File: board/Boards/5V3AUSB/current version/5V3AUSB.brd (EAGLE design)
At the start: 53.3 x 32.7 mm, 12 parts

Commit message: getting ready to add pads out +5V
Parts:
- added TP1, TP2: TP2P2-38-20, testpad:P2-38-20
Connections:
- net GND: now also TP1.TP-2, TP2.TP-2
- net N$3: now also TP1.TP-1, TP2.TP-1
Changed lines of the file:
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@@
 <element name="R1" library="resistor" package="R1206" value="250" x="11.43" y="2.54"/>
 <element name="U$1" library="Molex" package="2X2MOLEX" value="2X2-MOLEX" x="15.24" y="24.13" rot="R270"/>
+<element name="TP1" library="testpad" package="P2-38-20" value="TP2P2-38-20" x="-17.78" y="0">
+<attribute name="TP_SIGNAL_NAME" value="" x="-17.78" y="0" size="1.778" layer="27" display="off"/>
+</element>
+<element name="TP2" library="testpad" package="P2-38-20" value="TP2P2-38-20" x="-2.54" y="-17.78">
+<attribute name="TP_SIGNAL_NAME" value="" x="-2.54" y="-17.78" size="1.778" layer="27" display="off"/>
+</element>
 </elements>
 <signals>
@@
 <via x="29.21" y="22.86" extent="1-16" drill="0.6"/>
 <via x="29.21" y="21.59" extent="1-16" drill="0.6"/>
+<contactref element="TP1" pad="TP-2"/>
+<contactref element="TP2" pad="TP-2"/>
+<wire x1="-15.875" y1="0" x2="-0.635" y2="-17.78" width="0" layer="19" extent="1-1"/>
+<wire x1="10.008" y1="2.54" x2="-15.875" y2="0" width="0" layer="19" extent="1-1"/>
 </signal>
 <signal name="N$2">
@@
 <wire x1="29.21" y1="2.54" x2="29.21" y2="1.27" width="2.1844" layer="1"/>
 <via x="29.21" y="1.27" extent="1-16" drill="0.6"/>
+<contactref element="TP1" pad="TP-1"/>
+<contactref element="TP2" pad="TP-1"/>
+<wire x1="-19.685" y1="0" x2="-4.445" y2="-17.78" width="0" layer="19" extent="1-1"/>
+<wire x1="6.52" y1="12.39" x2="-19.685" y2="0" width="0" layer="19" extent="1-1"/>
 </signal>
 <signal name="N$6">

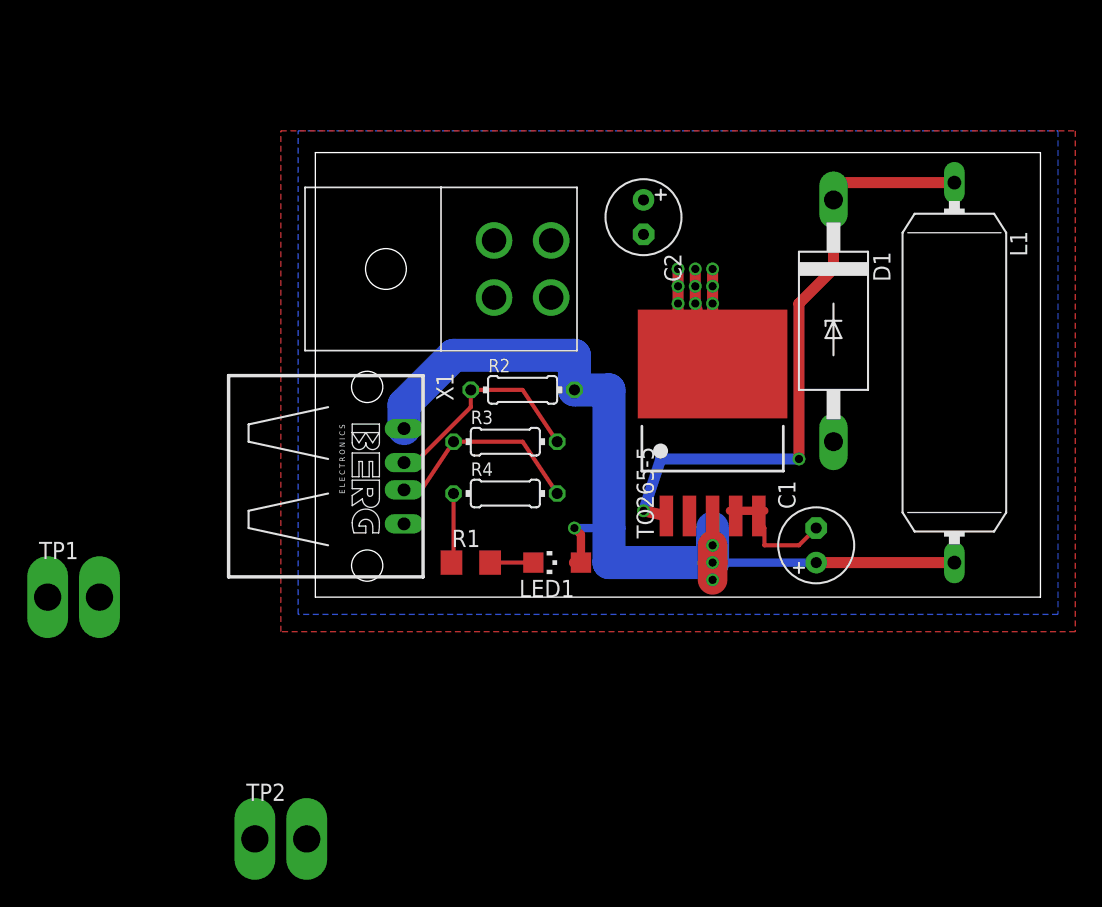
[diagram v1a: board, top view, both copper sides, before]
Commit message: board placement is looking good. going to verify schematic now
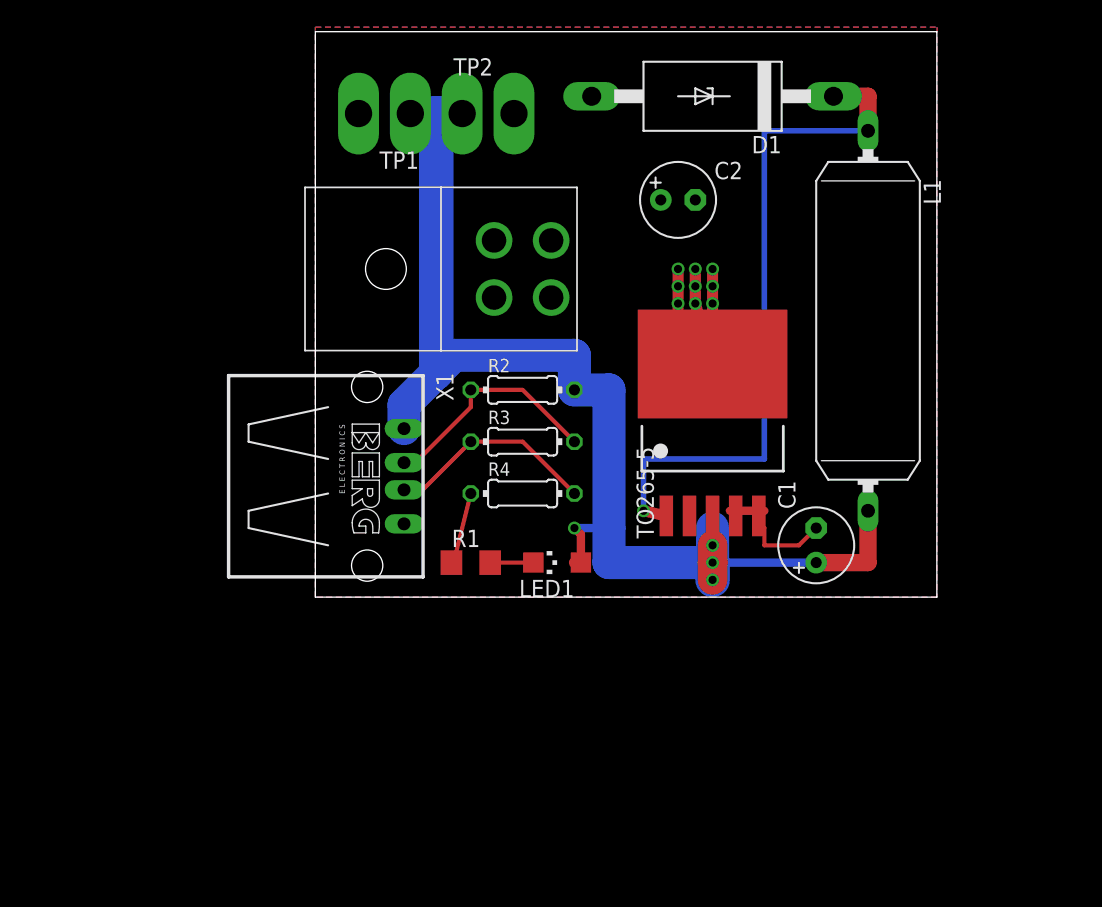
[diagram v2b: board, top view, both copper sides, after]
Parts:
- moved TP2 55.5 mm to (12.7, 35.6)
- moved TP1 42.3 mm to (5.08, 35.6), turned to 180 degrees
- moved D1 18.8 mm to (29.2, 36.8), turned to 180 degrees
- moved L1 7.41 mm to (40.6, 20.3)
- moved C2 2.84 mm to (26.7, 29.2), turned to 0 degrees
- moved R3 1.27 mm to (15.2, 11.4)
- moved R4 1.27 mm to (15.2, 7.62)
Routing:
- net N$3: track 72.0 -> 95.5 mm
- net N$2: track 46.2 -> 51.3 mm, vias 2 -> 1
- net N$7: track 16.2 -> 17.0 mm
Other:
- board size 53.3 x 32.7 mm -> 45.7 x 41.6 mm
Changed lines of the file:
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@@
 <board>
 <plain>
-<wire x1="0" y1="0" x2="53.32" y2="0" width="0" layer="20"/>
-<wire x1="53.32" y1="0" x2="53.32" y2="32.69" width="0" layer="20"/>
-<wire x1="53.32" y1="32.69" x2="0" y2="32.69" width="0" layer="20"/>
-<wire x1="0" y1="32.69" x2="0" y2="0" width="0" layer="20"/>
+<wire x1="0" y1="0" x2="45.7" y2="0" width="0" layer="20"/>
+<wire x1="45.7" y1="0" x2="45.7" y2="41.58" width="0" layer="20"/>
+<wire x1="45.7" y1="41.58" x2="0" y2="41.58" width="0" layer="20"/>
+<wire x1="0" y1="41.58" x2="0" y2="0" width="0" layer="20"/>
 </plain>
 <attributes>
@@
 <elements>
 <element name="C1" library="resistor" package="E2,5-6" value="220uF" x="36.83" y="3.81" rot="R90"/>
-<element name="C2" library="resistor" package="E2,5-6" value="470uF" x="24.13" y="27.94" rot="R270"/>
-<element name="D1" library="diode" package="CB429-17" value="15KEXX" x="38.1" y="20.32" rot="R270"/>
-<element name="L1" library="inductors" package="SUKW3-27" value="22uH" x="46.99" y="16.51" rot="R270"/>
+<element name="C2" library="resistor" package="E2,5-6" value="470uF" x="26.67" y="29.21"/>
+<element name="D1" library="diode" package="CB429-17" value="15KEXX" x="29.21" y="36.83" rot="R180"/>
+<element name="L1" library="inductors" package="SUKW3-27" value="22uH" x="40.64" y="20.32" rot="R270"/>
 <element name="TO265-5" library="on-semiconductor" package="TO263_5" value="CAT4101" x="29.21" y="13.97">
 <attribute name="OC_NEWARK" value="08R5264" x="48.26" y="3.81" size="1.778" layer="27" display="off"/>
@@
 <attribute name="SPICEPREFIX" value="R" x="15.24" y="15.24" size="1.778" layer="27" display="off"/>
 </element>
-<element name="R3" library="eagle-ltspice" package="0204/7" value="" x="13.97" y="11.43">
-<attribute name="SPICEMODEL" value="NONE" x="13.97" y="11.43" size="1.778" layer="27" display="off"/>
-<attribute name="SPICEPREFIX" value="R" x="13.97" y="11.43" size="1.778" layer="27" display="off"/>
-</element>
-<element name="R4" library="eagle-ltspice" package="0204/7" value="" x="13.97" y="7.62">
-<attribute name="SPICEMODEL" value="NONE" x="13.97" y="7.62" size="1.778" layer="27" display="off"/>
-<attribute name="SPICEPREFIX" value="R" x="13.97" y="7.62" size="1.778" layer="27" display="off"/>
+<element name="R3" library="eagle-ltspice" package="0204/7" value="" x="15.24" y="11.43">
+<attribute name="SPICEMODEL" value="NONE" x="15.24" y="11.43" size="1.778" layer="27" display="off"/>
+<attribute name="SPICEPREFIX" value="R" x="15.24" y="11.43" size="1.778" layer="27" display="off"/>
+</element>
+<element name="R4" library="eagle-ltspice" package="0204/7" value="" x="15.24" y="7.62">
+<attribute name="SPICEMODEL" value="NONE" x="15.24" y="7.62" size="1.778" layer="27" display="off"/>
+<attribute name="SPICEPREFIX" value="R" x="15.24" y="7.62" size="1.778" layer="27" display="off"/>
 </element>
 <element name="LED1" library="led" package="CHIPLED_1206" value="" x="17.78" y="2.54" rot="R90"/>
 <element name="R1" library="resistor" package="R1206" value="250" x="11.43" y="2.54"/>
 <element name="U$1" library="Molex" package="2X2MOLEX" value="2X2-MOLEX" x="15.24" y="24.13" rot="R270"/>
-<element name="TP1" library="testpad" package="P2-38-20" value="TP2P2-38-20" x="-17.78" y="0">
-<attribute name="TP_SIGNAL_NAME" value="" x="-17.78" y="0" size="1.778" layer="27" display="off"/>
-</element>
-<element name="TP2" library="testpad" package="P2-38-20" value="TP2P2-38-20" x="-2.54" y="-17.78">
-<attribute name="TP_SIGNAL_NAME" value="" x="-2.54" y="-17.78" size="1.778" layer="27" display="off"/>
+<element name="TP1" library="testpad" package="P2-38-20" value="TP2P2-38-20" x="5.08" y="35.56" rot="R180">
+<attribute name="TP_SIGNAL_NAME" value="" x="5.08" y="35.56" size="1.778" layer="27" rot="R180" display="off"/>
+</element>
+<element name="TP2" library="testpad" package="P2-38-20" value="TP2P2-38-20" x="12.7" y="35.56">
+<attribute name="TP_SIGNAL_NAME" value="" x="12.7" y="35.56" size="1.778" layer="27" display="off"/>
 </element>
 </elements>
@@
 <contactref element="U$1" pad="POWERR"/>
 <polygon width="0.4064" layer="1" isolate="0.4064" orphans="yes" thermals="no">
-<vertex x="-2.54" y="34.29"/>
-<vertex x="55.88" y="34.29"/>
-<vertex x="55.88" y="-2.54"/>
-<vertex x="-2.54" y="-2.54"/>
+<vertex x="0" y="41.91"/>
+<vertex x="45.72" y="41.91"/>
+<vertex x="45.72" y="0"/>
+<vertex x="0" y="0"/>
 </polygon>
 </signal>
@@
 <contactref element="U$1" pad="GNDL"/>
 <polygon width="0.4064" layer="16" isolate="0.4064" thermals="no">
-<vertex x="-1.27" y="34.29"/>
-<vertex x="54.61" y="34.29"/>
-<vertex x="54.61" y="-1.27"/>
-<vertex x="-1.27" y="-1.27"/>
+<vertex x="0" y="41.91"/>
+<vertex x="45.72" y="41.91"/>
+<vertex x="45.72" y="0"/>
+<vertex x="0" y="0"/>
 </polygon>
 <wire x1="29.21" y1="17.145" x2="27.94" y2="21.59" width="0.8128" layer="1"/>
@@
 <via x="27.94" y="22.86" extent="1-16" drill="0.6"/>
 <via x="27.94" y="21.59" extent="1-16" drill="0.6"/>
-<wire x1="10.16" y1="2.54" x2="10.16" y2="7.62" width="0.3048" layer="1"/>
+<wire x1="10.16" y1="2.54" x2="11.43" y2="7.62" width="0.3048" layer="1"/>
 <wire x1="10.16" y1="2.54" x2="10.008" y2="2.54" width="0.3048" layer="1"/>
 <wire x1="30.48" y1="6.35" x2="30.91" y2="5.97" width="0.3048" layer="1"/>
@@
 <contactref element="TP1" pad="TP-2"/>
 <contactref element="TP2" pad="TP-2"/>
-<wire x1="-15.875" y1="0" x2="-0.635" y2="-17.78" width="0" layer="19" extent="1-1"/>
-<wire x1="10.008" y1="2.54" x2="-15.875" y2="0" width="0" layer="19" extent="1-1"/>
 </signal>
 <signal name="N$2">
@@
 <contactref element="L1" pad="1"/>
 <contactref element="TO265-5" pad="1"/>
-<wire x1="38.1" y1="30.48" x2="46.99" y2="30.48" width="0.8128" layer="1"/>
-<wire x1="38.1" y1="29.21" x2="38.1" y2="30.48" width="0.8128" layer="1"/>
 <wire x1="24.13" y1="6.35" x2="25.81" y2="5.97" width="0.8128" layer="1"/>
-<wire x1="25.4" y1="10.16" x2="24.13" y2="6.35" width="0.8128" layer="16"/>
-<wire x1="35.56" y1="10.16" x2="25.4" y2="10.16" width="0.8128" layer="16"/>
-<wire x1="35.56" y1="21.59" x2="35.56" y2="10.16" width="0.8128" layer="1"/>
-<wire x1="38.1" y1="24.13" x2="35.56" y2="21.59" width="0.8128" layer="1"/>
-<wire x1="38.1" y1="29.21" x2="38.1" y2="24.13" width="0.8128" layer="1"/>
 <via x="24.13" y="6.35" extent="1-16" drill="0.6"/>
-<via x="35.56" y="10.16" extent="1-16" drill="0.6"/>
+<wire x1="40.64" y1="34.29" x2="40.64" y2="36.83" width="1.27" layer="1"/>
+<wire x1="40.64" y1="36.83" x2="38.1" y2="36.83" width="1.27" layer="1"/>
+<wire x1="40.64" y1="34.29" x2="33.02" y2="34.29" width="0.4064" layer="16"/>
+<wire x1="33.02" y1="34.29" x2="33.02" y2="10.16" width="0.4064" layer="16"/>
+<wire x1="33.02" y1="10.16" x2="24.13" y2="10.16" width="0.4064" layer="16"/>
+<wire x1="24.13" y1="10.16" x2="24.13" y2="6.35" width="0.4064" layer="16"/>
 </signal>
 <signal name="N$3">
@@
 <wire x1="29.21" y1="5.97" x2="29.21" y2="3.81" width="0.8128" layer="1"/>
 <wire x1="29.21" y1="3.81" x2="29.21" y2="2.54" width="2.1844" layer="1"/>
-<wire x1="46.99" y1="2.54" x2="36.83" y2="2.54" width="0.8128" layer="1"/>
 <wire x1="6.52" y1="12.39" x2="6.52" y2="14.14" width="2.43" layer="16"/>
-<wire x1="6.52" y1="14.14" x2="10.16" y2="17.78" width="2.43" layer="16"/>
+<wire x1="6.52" y1="14.14" x2="8.89" y2="16.51" width="2.43" layer="16"/>
+<wire x1="8.89" y1="16.51" x2="10.16" y2="17.78" width="2.43" layer="16"/>
 <wire x1="10.16" y1="17.78" x2="19.05" y2="17.78" width="2.43" layer="16"/>
 <wire x1="19.05" y1="17.78" x2="19.05" y2="15.24" width="2.43" layer="16"/>
@@
 <contactref element="TP1" pad="TP-1"/>
 <contactref element="TP2" pad="TP-1"/>
-<wire x1="-19.685" y1="0" x2="-4.445" y2="-17.78" width="0" layer="19" extent="1-1"/>
-<wire x1="6.52" y1="12.39" x2="-19.685" y2="0" width="0" layer="19" extent="1-1"/>
+<wire x1="6.985" y1="35.56" x2="10.795" y2="35.56" width="2.54" layer="16"/>
+<wire x1="36.83" y1="2.54" x2="40.64" y2="2.54" width="1.27" layer="1"/>
+<wire x1="40.64" y1="2.54" x2="40.64" y2="6.35" width="1.27" layer="1"/>
+<wire x1="10.795" y1="35.56" x2="8.89" y2="35.56" width="2.54" layer="16"/>
+<wire x1="8.89" y1="35.56" x2="8.89" y2="16.51" width="2.54" layer="16"/>
+<wire x1="29.21" y1="1.27" x2="29.21" y2="2.54" width="2.54" layer="16"/>
 </signal>
 <signal name="N$6">
@@
 <contactref element="X1" pad="3"/>
 <contactref element="R3" pad="1"/>
-<wire x1="15.24" y1="11.43" x2="17.78" y2="7.62" width="0.3048" layer="1"/>
-<wire x1="10.16" y1="11.43" x2="15.24" y2="11.43" width="0.3048" layer="1"/>
-<wire x1="7.62" y1="7.62" x2="10.16" y2="11.43" width="0.3048" layer="1"/>
+<wire x1="15.24" y1="11.43" x2="19.05" y2="7.62" width="0.3048" layer="1"/>
+<wire x1="11.43" y1="11.43" x2="15.24" y2="11.43" width="0.3048" layer="1"/>
+<wire x1="7.62" y1="7.62" x2="11.43" y2="11.43" width="0.3048" layer="1"/>
 <wire x1="7.62" y1="7.62" x2="6.52" y2="7.89" width="0.3048" layer="1"/>
 </signal>
@@
 <contactref element="X1" pad="2"/>
 <contactref element="R2" pad="1"/>
-<wire x1="17.78" y1="11.43" x2="15.24" y2="15.24" width="0.3048" layer="1"/>
+<wire x1="19.05" y1="11.43" x2="15.24" y2="15.24" width="0.3048" layer="1"/>
 <wire x1="11.43" y1="15.24" x2="15.24" y2="15.24" width="0.3048" layer="1"/>
 <wire x1="11.43" y1="13.97" x2="7.62" y2="10.16" width="0.3048" layer="1"/>
